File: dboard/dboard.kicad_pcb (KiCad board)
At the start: 2 copper layers, 53 x 11 mm, 17 parts, among them J1 Conn_01x04, U1 TPD2E2U06DRLR, U2 XC6206P332MR

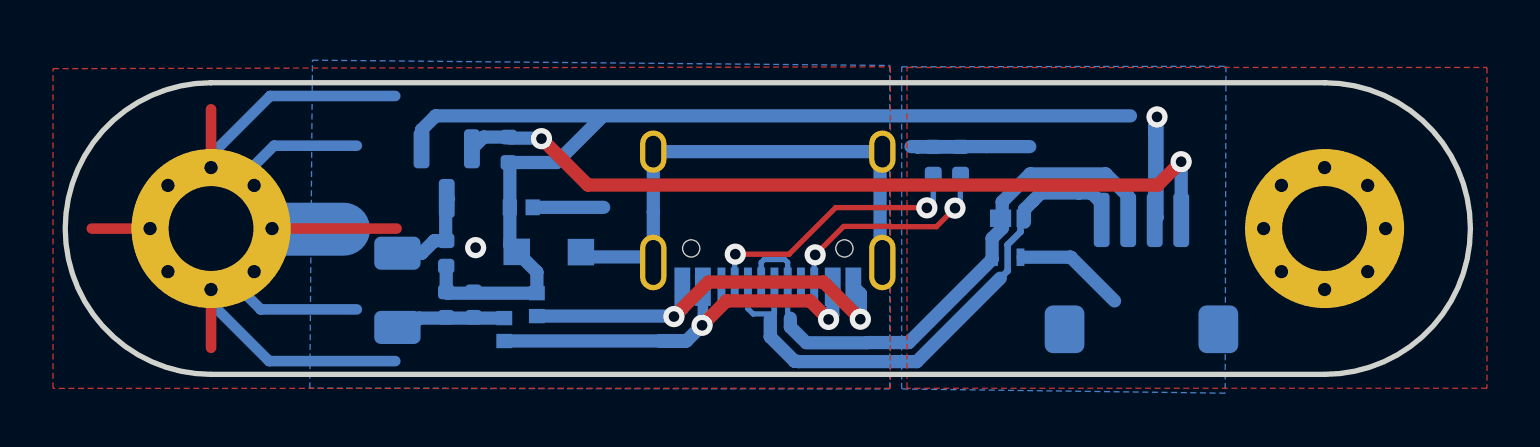
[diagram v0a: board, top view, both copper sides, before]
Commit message: added tvs
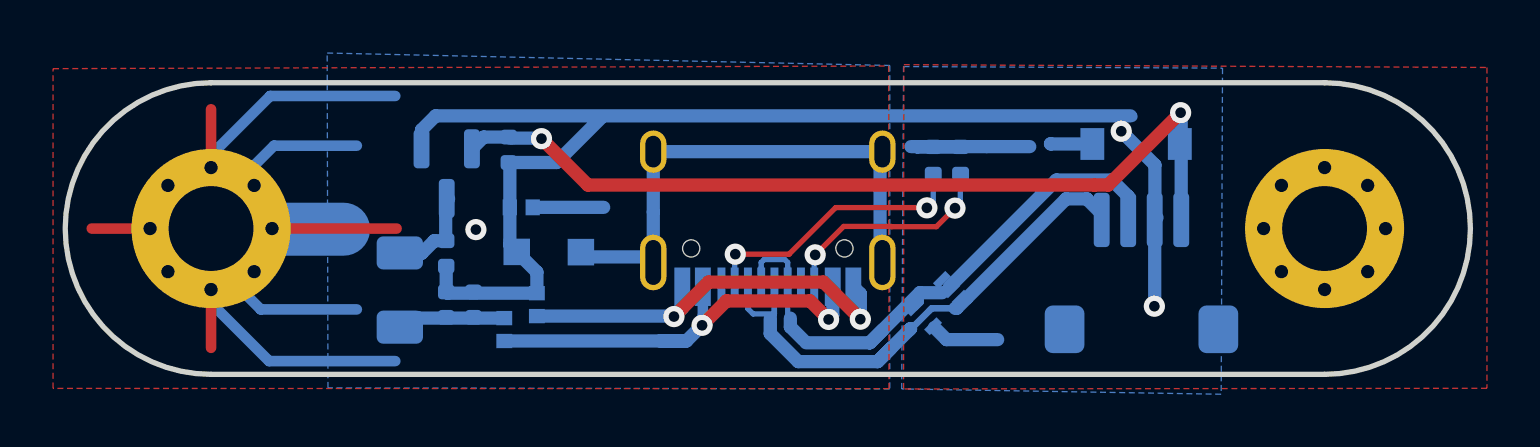
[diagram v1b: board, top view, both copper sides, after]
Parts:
- added D2: D_TVS, Diode_SMD:D_SOD-123, B.Cu at (13.9, 2.31)
- moved U1 3.60 mm to (6.40, 8.31), turned to -135 degrees
- moved F1 0.09 mm to (-13.9, 7.82)
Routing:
- net +3V3: track 30.2 -> 32.8 mm
- net GND: track 61.1 -> 59.9 mm, vias 1 -> 2
